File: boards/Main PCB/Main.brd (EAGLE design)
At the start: 160 x 101.3 mm, 67 parts, among them CN1 MINIB, CN2 MINIB, IC1 FT232RL, IC2 FT232RL, Q1 BSS138, Q2 BSS138, U1 MIC5225-3.3, U2 STM32F070CBT6, X1 JST-XH-06-PIN-LONG-PAD, X2 JST-XH-06-PIN-LONG-PAD, X3 JST-XH-04-PIN-LONG-PAD, X4 JST-XH-04-PIN-LONG-PAD, X5 JST-XH-04-PIN-LONG-PAD, X6 JST-XH-03-PIN-LONG-PAD, X7 JST-XH-03-PIN-LONG-PAD, Y1 32.768kHz

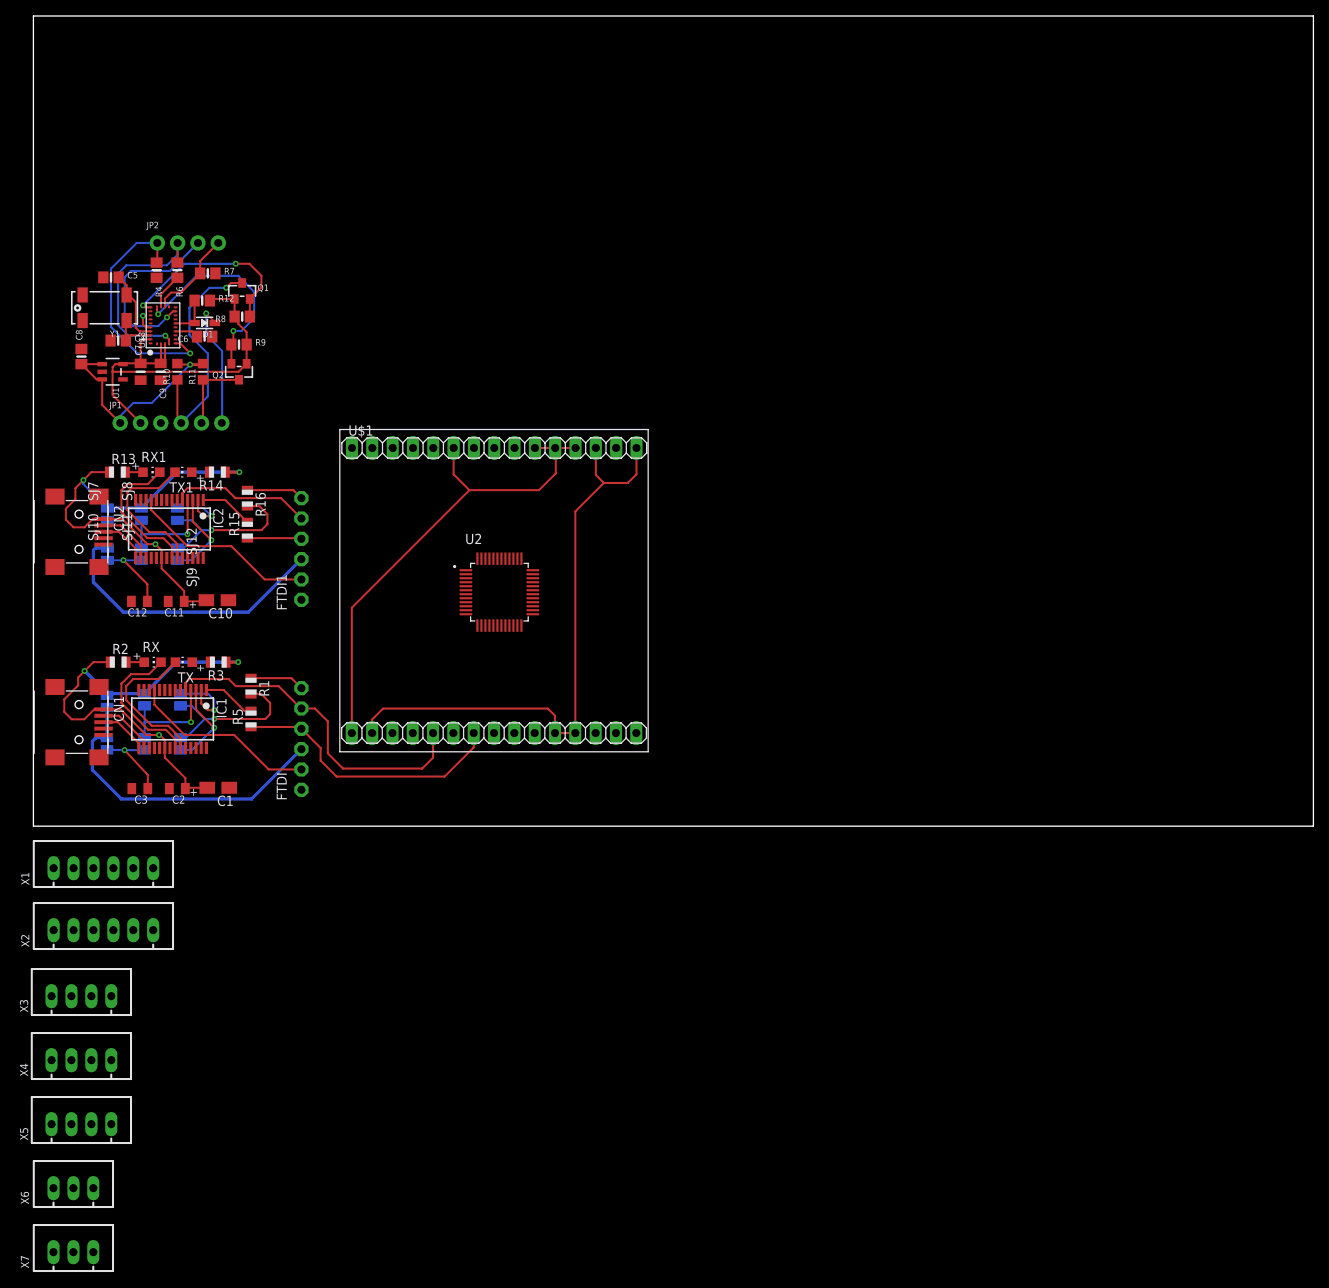
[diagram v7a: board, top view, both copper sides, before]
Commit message: Connected JSTs and arranged them in schematic
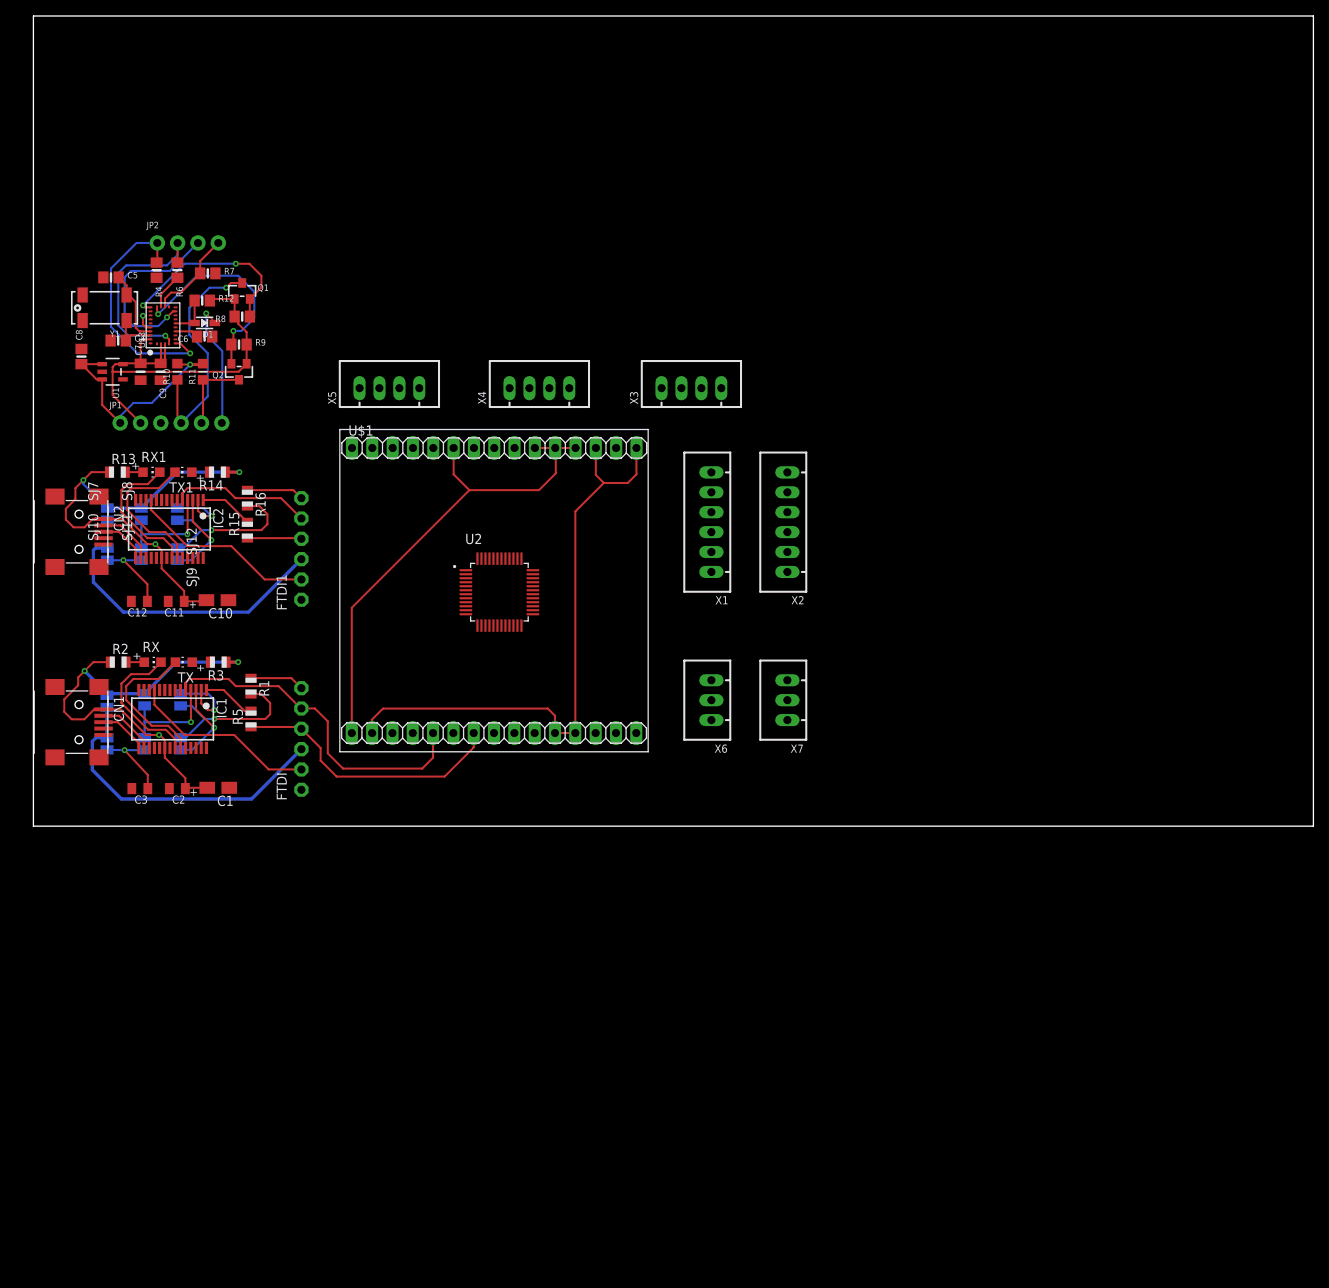
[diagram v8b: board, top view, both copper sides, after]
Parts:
- moved X7 112.8 mm to (94.2, 15.8), turned to 90 degrees
- moved X3 107.7 mm to (82.2, 54.8)
- moved X4 101.7 mm to (63.2, 54.8)
- moved X6 100.4 mm to (84.8, 15.8), turned to 90 degrees
- moved X5 99.7 mm to (44.5, 54.8)
- moved X2 99.6 mm to (94.2, 38.0), turned to 90 degrees
- moved X1 87.4 mm to (84.8, 38.0), turned to 90 degrees
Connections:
- new net N$21: U2.19, X7.2
- new net N$22: U2.14, X4.3
- new net N$23: U2.15, X4.2
- new net N$24: U2.10, X3.3
- new net N$25: U2.11, X3.2
- new net N$26: U2.16, X5.3
- new net N$27: U2.17, X5.2
- new net N$28: U2.12, X2.6
- new net N$29: U2.13, X2.5
- new net N$30: U2.25, X1.1
- new net N$31: U2.26, X1.2
- new net N$32: U2.27, X1.3
- new net N$33: U2.28, X1.4
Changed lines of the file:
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@@
 <attribute name="VALUE" x="24.464" y="41.762" size="1.27" layer="27" rot="R270"/>
 </element>
-<element name="X1" library="Rembrandt Electronics - JST XH Connectors v1-0" package="JST-XH-06-PACKAGE-LONG-PAD" value="JST-XH-06-PIN-LONG-PAD" x="8.75" y="-5.25" smashed="yes">
-<attribute name="NAME" x="-0.505" y="-7.39" size="1.016" layer="25" ratio="10" rot="R90"/>
-<attribute name="VALUE" x="0.4475" y="-1.3575" size="0.8128" layer="27" ratio="10"/>
+<element name="X1" library="Rembrandt Electronics - JST XH Connectors v1-0" package="JST-XH-06-PACKAGE-LONG-PAD" value="JST-XH-06-PIN-LONG-PAD" x="84.75" y="38" smashed="yes" rot="R90">
+<attribute name="NAME" x="86.89" y="28.745" size="1.016" layer="25" ratio="10" rot="R180"/>
+<attribute name="VALUE" x="80.8575" y="29.6975" size="0.8128" layer="27" ratio="10" rot="R90"/>
 </element>
-<element name="X2" library="Rembrandt Electronics - JST XH Connectors v1-0" package="JST-XH-06-PACKAGE-LONG-PAD" value="JST-XH-06-PIN-LONG-PAD" x="8.75" y="-13" smashed="yes">
-<attribute name="NAME" x="-0.505" y="-15.14" size="1.016" layer="25" ratio="10" rot="R90"/>
-<attribute name="VALUE" x="0.4475" y="-9.1075" size="0.8128" layer="27" ratio="10"/>
+<element name="X2" library="Rembrandt Electronics - JST XH Connectors v1-0" package="JST-XH-06-PACKAGE-LONG-PAD" value="JST-XH-06-PIN-LONG-PAD" x="94.25" y="38" smashed="yes" rot="R90">
+<attribute name="NAME" x="96.39" y="28.745" size="1.016" layer="25" ratio="10" rot="R180"/>
+<attribute name="VALUE" x="90.3575" y="29.6975" size="0.8128" layer="27" ratio="10" rot="R90"/>
 </element>
-<element name="X3" library="Rembrandt Electronics - JST XH Connectors v1-0" package="JST-XH-04-PACKAGE-LONG-PAD" value="JST-XH-04-PIN-LONG-PAD" x="6" y="-21.25" smashed="yes">
-<attribute name="NAME" x="-0.655" y="-23.29" size="1.016" layer="25" ratio="10" rot="R90"/>
-<attribute name="VALUE" x="-0.0025" y="-17.3575" size="1.016" layer="27" ratio="10"/>
+<element name="X3" library="Rembrandt Electronics - JST XH Connectors v1-0" package="JST-XH-04-PACKAGE-LONG-PAD" value="JST-XH-04-PIN-LONG-PAD" x="82.25" y="54.75" smashed="yes">
+<attribute name="NAME" x="75.595" y="52.71" size="1.016" layer="25" ratio="10" rot="R90"/>
+<attribute name="VALUE" x="76.2475" y="58.6425" size="1.016" layer="27" ratio="10"/>
 </element>
-<element name="X4" library="Rembrandt Electronics - JST XH Connectors v1-0" package="JST-XH-04-PACKAGE-LONG-PAD" value="JST-XH-04-PIN-LONG-PAD" x="6" y="-29.25" smashed="yes">
-<attribute name="NAME" x="-0.655" y="-31.29" size="1.016" layer="25" ratio="10" rot="R90"/>
-<attribute name="VALUE" x="-0.0025" y="-25.3575" size="1.016" layer="27" ratio="10"/>
+<element name="X4" library="Rembrandt Electronics - JST XH Connectors v1-0" package="JST-XH-04-PACKAGE-LONG-PAD" value="JST-XH-04-PIN-LONG-PAD" x="63.25" y="54.75" smashed="yes">
+<attribute name="NAME" x="56.595" y="52.71" size="1.016" layer="25" ratio="10" rot="R90"/>
+<attribute name="VALUE" x="57.2475" y="58.6425" size="1.016" layer="27" ratio="10"/>
 </element>
-<element name="X5" library="Rembrandt Electronics - JST XH Connectors v1-0" package="JST-XH-04-PACKAGE-LONG-PAD" value="JST-XH-04-PIN-LONG-PAD" x="6" y="-37.25" smashed="yes">
-<attribute name="NAME" x="-0.655" y="-39.29" size="1.016" layer="25" ratio="10" rot="R90"/>
-<attribute name="VALUE" x="-0.0025" y="-33.3575" size="1.016" layer="27" ratio="10"/>
+<element name="X5" library="Rembrandt Electronics - JST XH Connectors v1-0" package="JST-XH-04-PACKAGE-LONG-PAD" value="JST-XH-04-PIN-LONG-PAD" x="44.5" y="54.75" smashed="yes">
+<attribute name="NAME" x="37.845" y="52.71" size="1.016" layer="25" ratio="10" rot="R90"/>
+<attribute name="VALUE" x="38.4975" y="58.6425" size="1.016" layer="27" ratio="10"/>
 </element>
-<element name="X6" library="Rembrandt Electronics - JST XH Connectors v1-0" package="JST-XH-03-PACKAGE-LONG-PAD" value="JST-XH-03-PIN-LONG-PAD" x="5" y="-45.25" smashed="yes">
-<attribute name="NAME" x="-0.555" y="-47.29" size="1.016" layer="25" ratio="10" rot="R90"/>
-<attribute name="VALUE" x="0.3975" y="-41.3575" size="1.016" layer="27" ratio="10"/>
+<element name="X6" library="Rembrandt Electronics - JST XH Connectors v1-0" package="JST-XH-03-PACKAGE-LONG-PAD" value="JST-XH-03-PIN-LONG-PAD" x="84.75" y="15.75" smashed="yes" rot="R90">
+<attribute name="NAME" x="86.79" y="10.195" size="1.016" layer="25" ratio="10" rot="R180"/>
+<attribute name="VALUE" x="80.8575" y="11.1475" size="1.016" layer="27" ratio="10" rot="R90"/>
 </element>
-<element name="X7" library="Rembrandt Electronics - JST XH Connectors v1-0" package="JST-XH-03-PACKAGE-LONG-PAD" value="JST-XH-03-PIN-LONG-PAD" x="5" y="-53.25" smashed="yes">
-<attribute name="NAME" x="-0.555" y="-55.29" size="1.016" layer="25" ratio="10" rot="R90"/>
-<attribute name="VALUE" x="0.3975" y="-49.3575" size="1.016" layer="27" ratio="10"/>
+<element name="X7" library="Rembrandt Electronics - JST XH Connectors v1-0" package="JST-XH-03-PACKAGE-LONG-PAD" value="JST-XH-03-PIN-LONG-PAD" x="94.25" y="15.75" smashed="yes" rot="R90">
+<attribute name="NAME" x="96.29" y="10.195" size="1.016" layer="25" ratio="10" rot="R180"/>
+<attribute name="VALUE" x="90.3575" y="11.1475" size="1.016" layer="27" ratio="10" rot="R90"/>
 </element>
 <element name="U2" library="STM32F070CBT6" package="QFP50P900X900X160-48N" value="STM32F070CBT6" x="58.25" y="29.25" smashed="yes">
@@
 <contactref element="U2" pad="8"/>
 </signal>
+<signal name="N$22">
+<contactref element="U2" pad="14"/>
+<contactref element="X4" pad="3"/>
+<wire x1="56" y1="25.07" x2="64.4946" y2="54.75" width="0" layer="19" extent="1-1"/>
+</signal>
+<signal name="N$23">
+<contactref element="X4" pad="2"/>
+<contactref element="U2" pad="15"/>
+<wire x1="56.5" y1="25.07" x2="62.0054" y2="54.75" width="0" layer="19" extent="1-1"/>
+</signal>
+<signal name="N$24">
+<contactref element="U2" pad="10"/>
+<contactref element="X3" pad="3"/>
+<wire x1="54.07" y1="27.5" x2="83.4946" y2="54.75" width="0" layer="19" extent="1-1"/>
+</signal>
+<signal name="N$25">
+<contactref element="U2" pad="11"/>
+<contactref element="X3" pad="2"/>
+<wire x1="54.07" y1="27" x2="81.0054" y2="54.75" width="0" layer="19" extent="1-1"/>
+</signal>
+<signal name="N$26">
+<contactref element="U2" pad="16"/>
+<contactref element="X5" pad="3"/>
+<wire x1="57" y1="25.07" x2="45.7446" y2="54.75" width="0" layer="19" extent="1-1"/>
+</signal>
+<signal name="N$27">
+<contactref element="U2" pad="17"/>
+<contactref element="X5" pad="2"/>
+<wire x1="57.5" y1="25.07" x2="43.2554" y2="54.75" width="0" layer="19" extent="1-1"/>
+</signal>
 <signal name="N$20">
 <contactref element="U2" pad="18"/>
 <contactref element="X6" pad="2"/>
-<wire x1="5" y1="-45.25" x2="58" y2="25.07" width="0" layer="19" extent="1-1"/>
+<wire x1="58" y1="25.07" x2="84.75" y2="15.75" width="0" layer="19" extent="1-1"/>
+</signal>
+<signal name="N$21">
+<contactref element="U2" pad="19"/>
+<contactref element="X7" pad="2"/>
+<wire x1="58.5" y1="25.07" x2="94.25" y2="15.75" width="0" layer="19" extent="1-1"/>
+</signal>
+<signal name="N$28">
+<contactref element="U2" pad="12"/>
+<contactref element="X2" pad="6"/>
+<wire x1="54.07" y1="26.5" x2="94.25" y2="44.223" width="0" layer="19" extent="1-1"/>
+</signal>
+<signal name="N$29">
+<contactref element="U2" pad="13"/>
+<contactref element="X2" pad="5"/>
+<wire x1="55.5" y1="25.07" x2="94.25" y2="41.7338" width="0" layer="19" extent="1-1"/>
+</signal>
+<signal name="N$30">
+<contactref element="U2" pad="25"/>
+<contactref element="X1" pad="1"/>
+<wire x1="62.43" y1="26.5" x2="84.75" y2="31.777" width="0" layer="19" extent="1-1"/>
+</signal>
+<signal name="N$31">
+<contactref element="U2" pad="26"/>
+<contactref element="X1" pad="2"/>
+<wire x1="62.43" y1="27" x2="84.75" y2="34.2662" width="0" layer="19" extent="1-1"/>
+</signal>
+<signal name="N$32">
+<contactref element="U2" pad="27"/>
+<contactref element="X1" pad="3"/>
+<wire x1="62.43" y1="27.5" x2="84.75" y2="36.7554" width="0" layer="19" extent="1-1"/>
+</signal>
+<signal name="N$33">
+<contactref element="U2" pad="28"/>
+<contactref element="X1" pad="4"/>
+<wire x1="62.43" y1="28" x2="84.75" y2="39.2446" width="0" layer="19" extent="1-1"/>
 </signal>
 </signals>
